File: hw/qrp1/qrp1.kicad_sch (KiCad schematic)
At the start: 45 parts, among them J1 Conn_Coaxial, J2 Conn_Coaxial, J3 Conn_01x02, J4 Conn_01x02, Q1 2N3904, Q2 2N2219, T1 Bifilar Toroid, T2 Bifilar Toroid, U1 MC78L06_TO92, U2 IRF510PBF

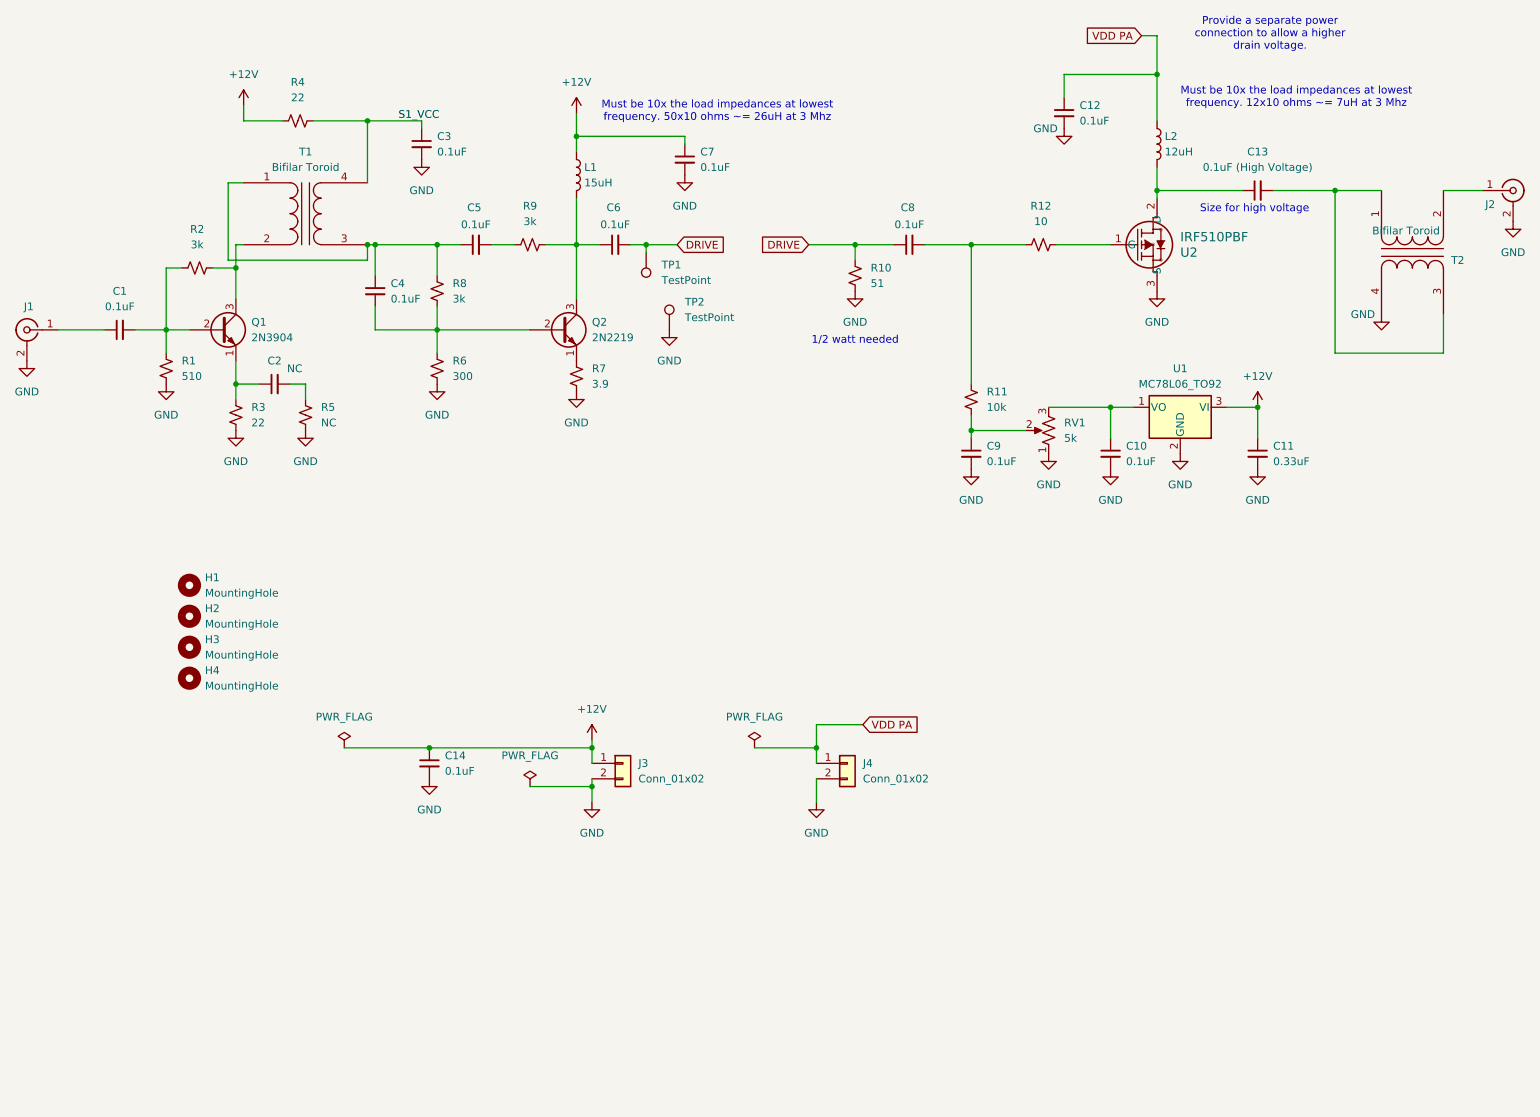
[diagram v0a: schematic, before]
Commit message: Added power enable control on driver stages
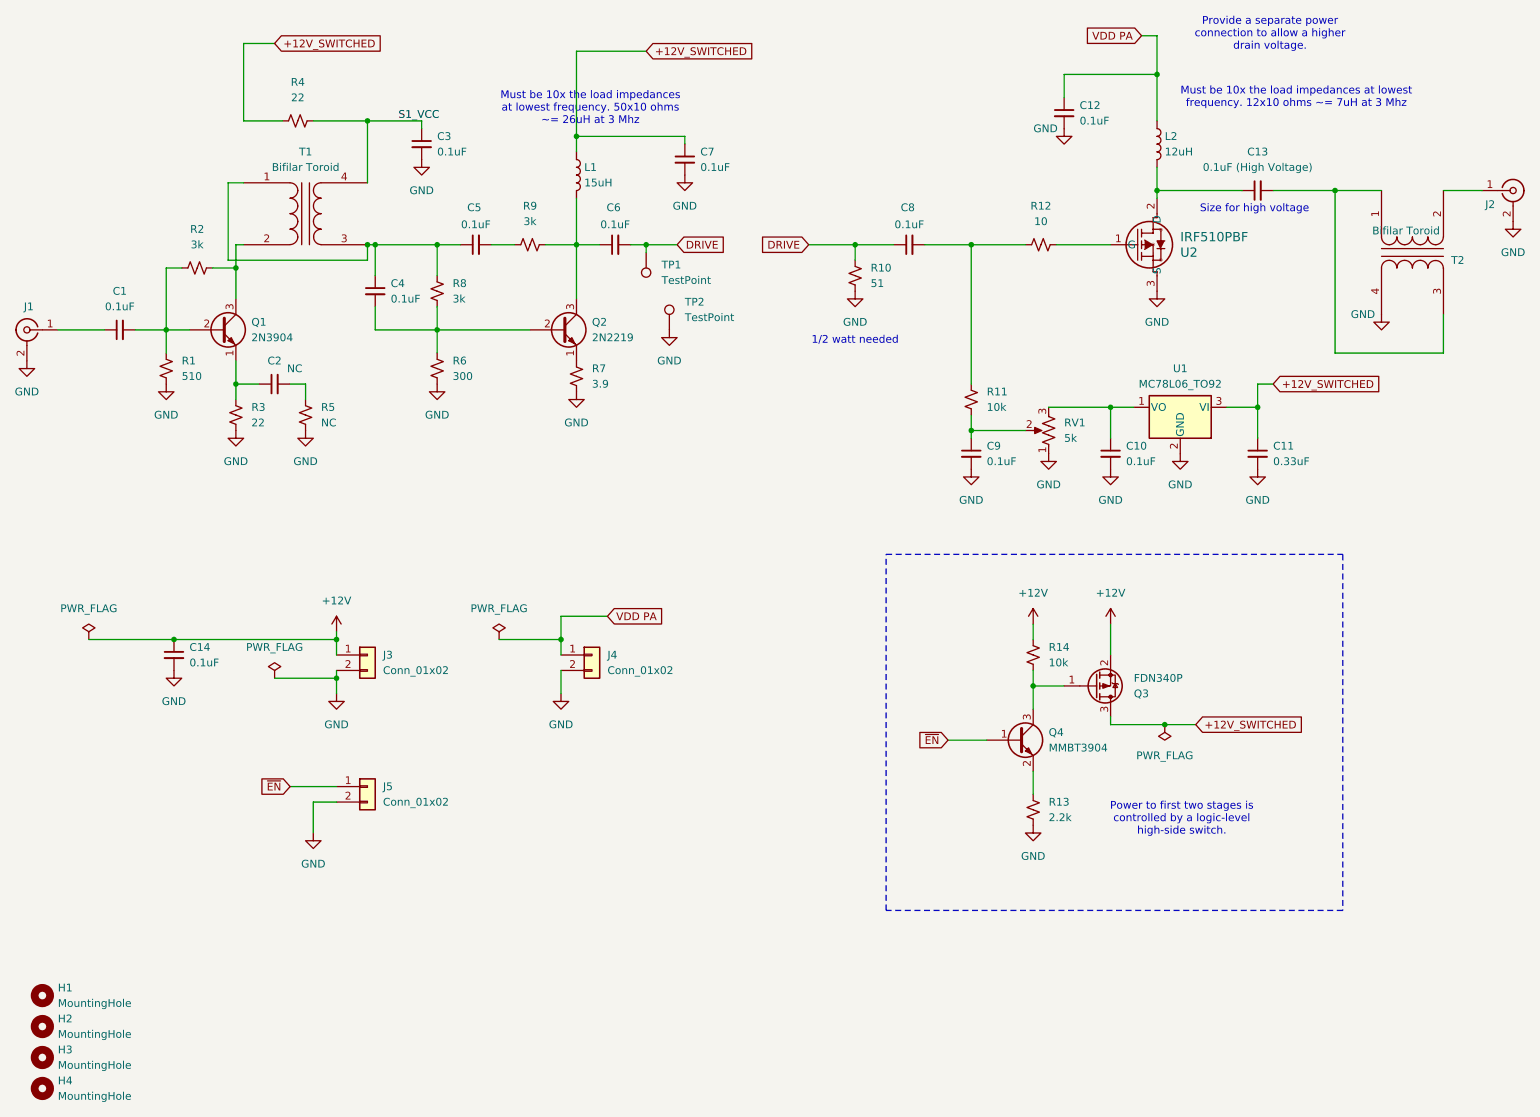
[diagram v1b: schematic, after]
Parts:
- added J5: Conn_01x02, Connector_PinHeader_2.54mm:PinHeader_1x02_P2.54mm_Vertical, symbol Connector_Generic:Conn_01x02
- added Q3: FDN340P, Package_TO_SOT_SMD:SOT-23, symbol Transistor_FET:FDN340P
- added Q4: MMBT3904, Package_TO_SOT_SMD:SOT-23, symbol Transistor_BJT:MMBT3904
- added R13: 2.2k, Resistor_SMD:R_0805_2012Metric_Pad1.20x1.40mm_HandSolder, symbol Device:R_Small_US
- added R14: 10k, Resistor_SMD:R_0805_2012Metric_Pad1.20x1.40mm_HandSolder, symbol Device:R_Small_US
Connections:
- net +12V: now also Q3.2 (S), R14.1; no longer C11.1, C7.1, L1.1, R4.1, U1.3 (VI)
- net GND: now also J5.2 (Pin_2), R13.2
- new net: Q4.2 (E), R13.1
- new net: Q3.1 (G), Q4.3 (C), R14.2
- new net +12V_SWITCHED: C11.1, C7.1, L1.1, Q3.3 (D), R4.1, U1.3 (VI)
- new net ~{EN}: J5.1 (Pin_1), Q4.1 (B)
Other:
- note added: "Power to first two stages is controlled by a logic-level high-side switch."
- moved on the sheet: C14, H1, H2, H3, H4, J3, J4
